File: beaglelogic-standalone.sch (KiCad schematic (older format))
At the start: 252 parts, among them J1 USB_OTG, J2 CONN_02X02, J3 USB_A, J4 CONN_01X06, J5 SI-51009-F, J6 CONN_02X12, J7 CONN_02X16, J8 Barrel_Jack, M1 TEST_1P, M2 TEST_1P, M3 TEST_1P, M4 TEST_1P, Q1 BSS138, Q2 BSS138, SW1 SW_PUSH_SMALL_H, SW2 SW_PUSH_SMALL_H, U1 74LVC1G07, U10 MCP79410/TDFN, U11 SST26VF064B, U12 TPS73101, U13 SN74LVCH16T245, U14 DVIULC6-4SC6, U15 DVIULC6-4SC6, U16 DVIULC6-4SC6, U17 DVIULC6-4SC6, U18 74LV1T125, U19 EMMC_4G, U2 AP1117, U3 TPS2051C, U4 TPD4S012, U5 TPD4S012, U6 OSD3358-SM, U7 KSZ9031RNXCC, U8 74LVC2G241, U9 74LVC1G125, Y1 25MHz, Y2 24MHz, Y3 32.768kHz,CL=9pF

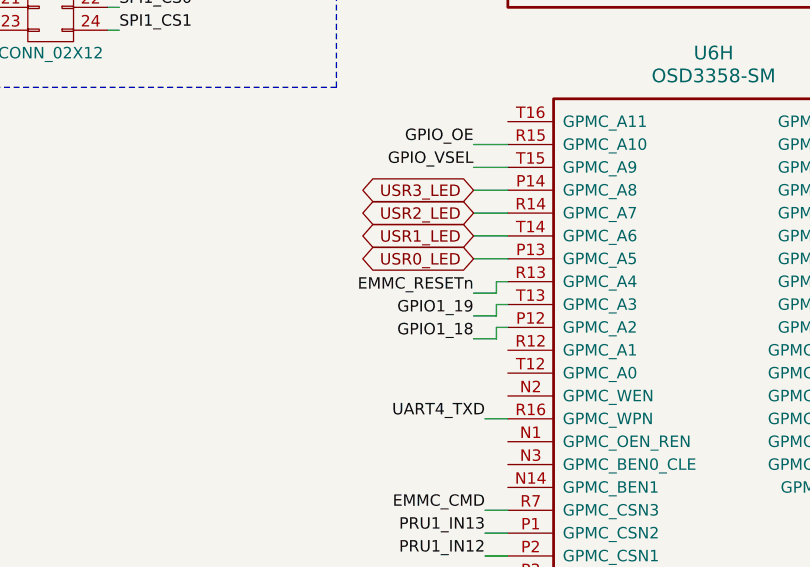
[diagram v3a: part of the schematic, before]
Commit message: Route the eMMC
Signed-off-by: Kumar Abhishek <abhishek@theembeddedkitchen.net>
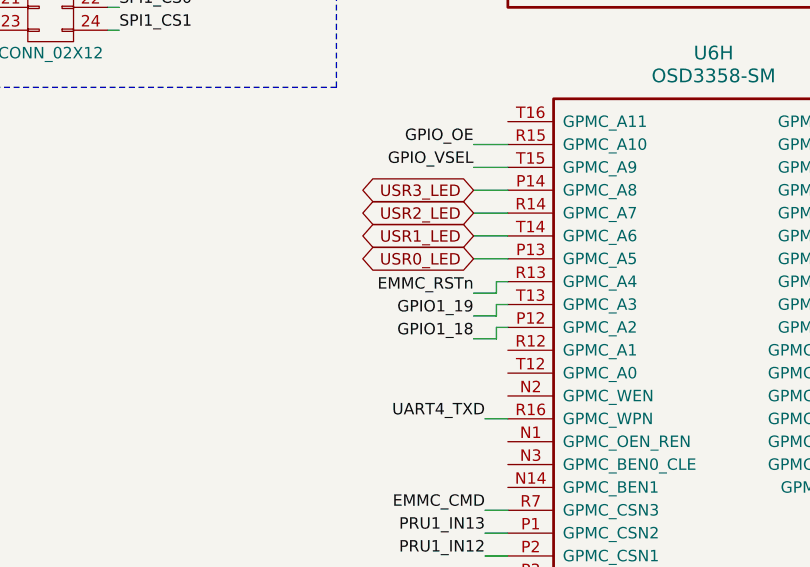
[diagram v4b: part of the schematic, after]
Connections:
- net EMMC_RESETn is gone; now on net EMMC_RSTn: U6.R13 (GPMC_A4)
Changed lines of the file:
@@
 GPIO_OE
 Text Label 9200 7200 2    50   ~ 0
-EMMC_RESETn
+EMMC_RSTn
 Text Label 12550 2700 2    50   ~ 0
 SPIF_CS

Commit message: Finish routing
Signed-off-by: Kumar Abhishek <abhishek@theembeddedkitchen.net>
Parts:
- added C65, C66: 0.1uF, Capacitors_SMD:C_0402, symbol C_Small
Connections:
- net +3V3: now also C65.2
- net DIN00: now also U14.4 (X3); no longer U14.1 (X1)
- net DIN03: now also U14.1 (X1); no longer U14.4 (X3)
- net DIN04: now also U15.4 (X3); no longer U15.1 (X1)
- net DIN07: now also U15.1 (X1); no longer U15.4 (X3)
- net DIN08: now also U16.4 (X3); no longer U16.1 (X1)
- net DIN11: now also U16.1 (X1); no longer U16.4 (X3)
- net DIN12: now also U17.4 (X3); no longer U17.1 (X1)
- net DIN15: now also U17.1 (X1); no longer U17.4 (X3)
- net GND: now also C65.1, C66.1
- net at C42.2, R58.1, U12.5 (VOUT)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: now also C66.2
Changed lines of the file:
@@
 	1    0    0    -1
 $EndComp
-Text Label 17900 5150 2    50   ~ 0
+Text Label 18800 5450 0    50   ~ 0
 DIN00
 Text Label 18800 5150 0    50   ~ 0
@@
 Text Label 17900 5450 2    50   ~ 0
 DIN02
-Text Label 18800 5450 0    50   ~ 0
+Text Label 17900 5150 2    50   ~ 0
 DIN03
-Text Label 17900 6000 2    50   ~ 0
+Text Label 18800 6300 0    50   ~ 0
 DIN04
 Text Label 18800 6000 0    50   ~ 0
@@
 Text Label 17900 6300 2    50   ~ 0
 DIN06
-Text Label 18800 6300 0    50   ~ 0
+Text Label 17900 6000 2    50   ~ 0
 DIN07
-Text Label 17900 6850 2    50   ~ 0
+Text Label 18800 7150 0    50   ~ 0
 DIN08
 Text Label 18800 6850 0    50   ~ 0
@@
 Text Label 17900 7150 2    50   ~ 0
 DIN10
-Text Label 18800 7150 0    50   ~ 0
+Text Label 17900 6850 2    50   ~ 0
 DIN11
-Text Label 17900 7750 2    50   ~ 0
+Text Label 18800 8050 0    50   ~ 0
 DIN12
 Text Label 18800 7750 0    50   ~ 0
 DIN13
-Text Label 18800 8050 0    50   ~ 0
+Text Label 17900 7750 2    50   ~ 0
 DIN15
 Text Label 17900 8050 2    50   ~ 0
@@
 L GND #PWR026
 U 1 1 59699004
-P 15000 5400
-F 0 "#PWR026" H 15000 5150 50  0001 C CNN
-F 1 "GND" H 15005 5227 50  0000 C CNN
-F 2 "" H 15000 5400 50  0001 C CNN
-F 3 "" H 15000 5400 50  0001 C CNN
-	1    15000 5400
+P 15000 5550
+F 0 "#PWR026" H 15000 5300 50  0001 C CNN
+F 1 "GND" H 15005 5377 50  0000 C CNN
+F 2 "" H 15000 5550 50  0001 C CNN
+F 3 "" H 15000 5550 50  0001 C CNN
+	1    15000 5550
 	1    0    0    -1
 $EndComp
@@
 	16700 4950 16700 5350
 Wire Wire Line
-	16400 5350 17100 5350
+	16400 5350 17300 5350
 Wire Wire Line
 	16400 5350 16400 5300
@@
 Connection ~ 16800 5350
 Wire Wire Line
-	17200 5000 17100 5000
+	17100 5000 17300 5000
 Wire Wire Line
 	17100 5000 17100 5100
@@
 Connection ~ 15300 5250
 Wire Wire Line
-	15000 5250 15000 5400
+	15000 5250 15000 5550
 Connection ~ 13300 5250
 Wire Wire Line
@@
 	1    0    0    -1
 $EndComp
+$Comp
+L C_Small C66
+U 1 1 59B026E5
+P 17300 5200
+F 0 "C66" H 17186 5154 50  0000 R CNN
+F 1 "0.1uF" H 17186 5245 50  0000 R CNN
+F 2 "Capacitors_SMD:C_0402" H 17338 5050 50  0001 C CNN
+F 3 "" H 17300 5200 50  0001 C CNN
+	1    17300 5200
+	-1   0    0    1
+$EndComp
+Wire Wire Line
+	17300 5000 17300 5100
+Wire Wire Line
+	17300 5350 17300 5300
+Connection ~ 17100 5350
+$Comp
+L C_Small C65
+U 1 1 59B047BC
+P 15150 5400
+F 0 "C65" V 14950 5400 50  0000 C CNN
+F 1 "0.1uF" V 15050 5400 50  0000 C CNN
+F 2 "Capacitors_SMD:C_0402" H 15188 5250 50  0001 C CNN
+F 3 "" H 15150 5400 50  0001 C CNN
+	1    15150 5400
+	0    -1   -1   0
+$EndComp
+Wire Wire Line
+	15050 5400 15000 5400
+Connection ~ 15000 5400
+Wire Wire Line
+	15250 5400 15300 5400
+Connection ~ 15300 5400
 $EndSCHEMATC

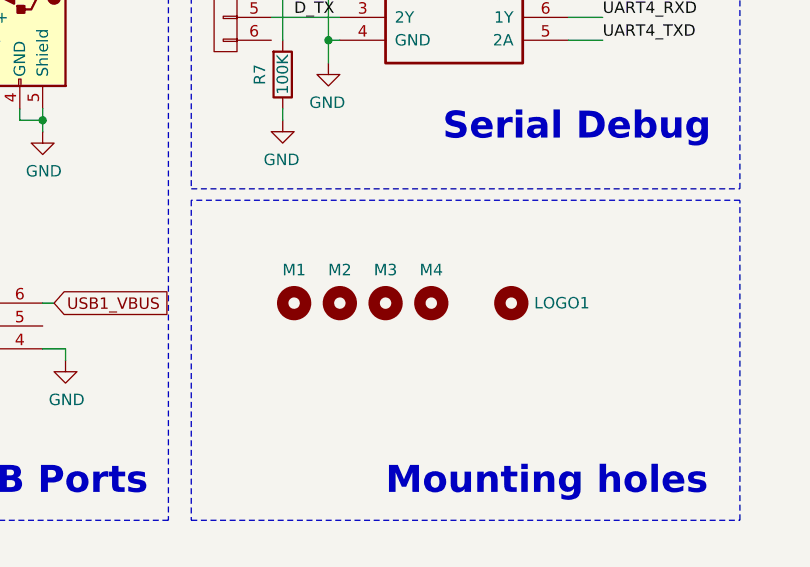
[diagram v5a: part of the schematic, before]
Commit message: Final touches to Rev A
 * Shrink logo to fit on board
 * Add fiducials on board
 * Rotate USB-A connector 90 degrees so that it does not interfere with
   microUSB
 * Add helper text

Signed-off-by: Kumar Abhishek <abhishek@theembeddedkitchen.net>
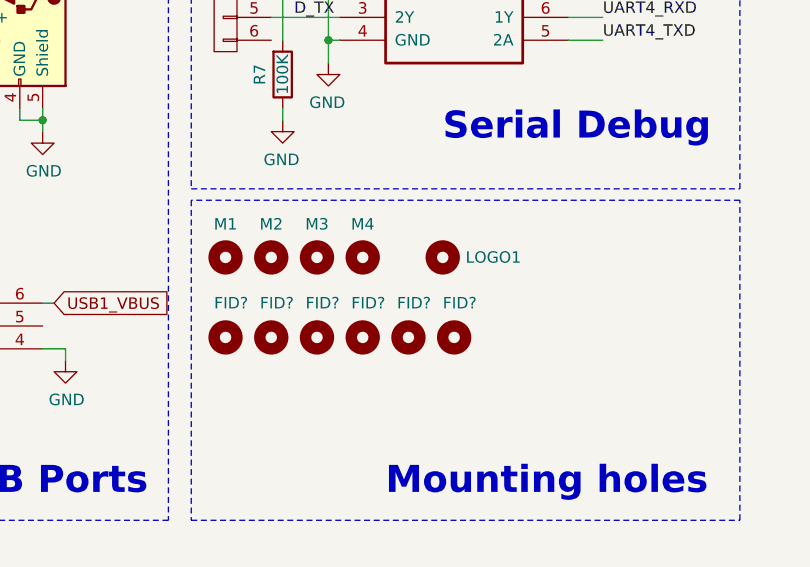
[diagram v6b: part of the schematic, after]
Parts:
- added FID? (x6): Mounting_Hole, Fiducials:Fiducial_1mm_Dia_2.54mm_Outer_CopperTop, symbol Mounting_Hole
- D1, D2, D3, D4: value LED -> GREEN
- R104, R106, R108, R110, R112, R114, R116, R118, R66, R68, R70, R72, R74, R76, R78, R80, R82: value 1M,DNI -> 1M,S
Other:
- moved on the sheet: LOGO1, M1, M2, M3, M4
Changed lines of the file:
@@
 P 19600 5200
 F 0 "R66" V 19600 5250 50  0000 R CNN
-F 1 "1M,DNI" V 19700 5300 50  0001 R CNN
+F 1 "1M,S" V 19700 5300 50  0001 R CNN
 F 2 "Resistors_SMD:R_0402" V 19530 5200 50  0001 C CNN
 F 3 "" H 19600 5200 50  0001 C CNN
@@
 P 19600 5650
 F 0 "R68" V 19600 5700 50  0000 R CNN
-F 1 "1M,DNI" V 19700 5750 50  0001 R CNN
+F 1 "1M,S" V 19700 5750 50  0001 R CNN
 F 2 "Resistors_SMD:R_0402" V 19530 5650 50  0001 C CNN
 F 3 "" H 19600 5650 50  0001 C CNN
@@
 P 19600 6100
 F 0 "R70" V 19600 6150 50  0000 R CNN
-F 1 "1M,DNI" V 19700 6200 50  0001 R CNN
+F 1 "1M,S" V 19700 6200 50  0001 R CNN
 F 2 "Resistors_SMD:R_0402" V 19530 6100 50  0001 C CNN
 F 3 "" H 19600 6100 50  0001 C CNN
@@
 P 19600 6550
 F 0 "R72" V 19600 6600 50  0000 R CNN
-F 1 "1M,DNI" V 19700 6650 50  0001 R CNN
+F 1 "1M,S" V 19700 6650 50  0001 R CNN
 F 2 "Resistors_SMD:R_0402" V 19530 6550 50  0001 C CNN
 F 3 "" H 19600 6550 50  0001 C CNN
@@
 P 19600 7000
 F 0 "R74" V 19600 7050 50  0000 R CNN
-F 1 "1M,DNI" V 19700 7100 50  0001 R CNN
+F 1 "1M,S" V 19700 7100 50  0001 R CNN
 F 2 "Resistors_SMD:R_0402" V 19530 7000 50  0001 C CNN
 F 3 "" H 19600 7000 50  0001 C CNN
@@
 P 19600 7450
 F 0 "R76" V 19600 7500 50  0000 R CNN
-F 1 "1M,DNI" V 19700 7550 50  0001 R CNN
+F 1 "1M,S" V 19700 7550 50  0001 R CNN
 F 2 "Resistors_SMD:R_0402" V 19530 7450 50  0001 C CNN
 F 3 "" H 19600 7450 50  0001 C CNN
@@
 P 19600 7900
 F 0 "R78" V 19600 7950 50  0000 R CNN
-F 1 "1M,DNI" V 19700 8000 50  0001 R CNN
+F 1 "1M,S" V 19700 8000 50  0001 R CNN
 F 2 "Resistors_SMD:R_0402" V 19530 7900 50  0001 C CNN
 F 3 "" H 19600 7900 50  0001 C CNN
@@
 P 19600 8350
 F 0 "R80" V 19600 8400 50  0000 R CNN
-F 1 "1M,DNI" V 19700 8450 50  0001 R CNN
+F 1 "1M,S" V 19700 8450 50  0001 R CNN
 F 2 "Resistors_SMD:R_0402" V 19530 8350 50  0001 C CNN
 F 3 "" H 19600 8350 50  0001 C CNN
@@
 P 20900 5200
 F 0 "R104" V 20900 5250 50  0000 R CNN
-F 1 "1M,DNI" V 21000 5300 50  0001 R CNN
+F 1 "1M,S" V 21000 5300 50  0001 R CNN
 F 2 "Resistors_SMD:R_0402" V 20830 5200 50  0001 C CNN
 F 3 "" H 20900 5200 50  0001 C CNN
@@
 P 20900 5650
 F 0 "R106" V 20900 5700 50  0000 R CNN
-F 1 "1M,DNI" V 21000 5750 50  0001 R CNN
+F 1 "1M,S" V 21000 5750 50  0001 R CNN
 F 2 "Resistors_SMD:R_0402" V 20830 5650 50  0001 C CNN
 F 3 "" H 20900 5650 50  0001 C CNN
@@
 P 20900 6100
 F 0 "R108" V 20900 6150 50  0000 R CNN
-F 1 "1M,DNI" V 21000 6200 50  0001 R CNN
+F 1 "1M,S" V 21000 6200 50  0001 R CNN
 F 2 "Resistors_SMD:R_0402" V 20830 6100 50  0001 C CNN
 F 3 "" H 20900 6100 50  0001 C CNN
@@
 P 20900 6550
 F 0 "R110" V 20900 6600 50  0000 R CNN
-F 1 "1M,DNI" V 21000 6650 50  0001 R CNN
+F 1 "1M,S" V 21000 6650 50  0001 R CNN
 F 2 "Resistors_SMD:R_0402" V 20830 6550 50  0001 C CNN
 F 3 "" H 20900 6550 50  0001 C CNN
@@
 P 20900 7000
 F 0 "R112" V 20900 7050 50  0000 R CNN
-F 1 "1M,DNI" V 21000 7100 50  0001 R CNN
+F 1 "1M,S" V 21000 7100 50  0001 R CNN
 F 2 "Resistors_SMD:R_0402" V 20830 7000 50  0001 C CNN
 F 3 "" H 20900 7000 50  0001 C CNN
@@
 P 20900 7450
 F 0 "R114" V 20900 7500 50  0000 R CNN
-F 1 "1M,DNI" V 21000 7550 50  0001 R CNN
+F 1 "1M,S" V 21000 7550 50  0001 R CNN
 F 2 "Resistors_SMD:R_0402" V 20830 7450 50  0001 C CNN
 F 3 "" H 20900 7450 50  0001 C CNN
@@
 P 20900 7900
 F 0 "R116" V 20900 7950 50  0000 R CNN
-F 1 "1M,DNI" V 21000 8000 50  0001 R CNN
+F 1 "1M,S" V 21000 8000 50  0001 R CNN
 F 2 "Resistors_SMD:R_0402" V 20830 7900 50  0001 C CNN
 F 3 "" H 20900 7900 50  0001 C CNN
@@
 P 20900 8350
 F 0 "R118" V 20900 8400 50  0000 R CNN
-F 1 "1M,DNI" V 21000 8450 50  0001 R CNN
+F 1 "1M,S" V 21000 8450 50  0001 R CNN
 F 2 "Resistors_SMD:R_0402" V 20830 8350 50  0001 C CNN
 F 3 "" H 20900 8350 50  0001 C CNN
@@
 P 6000 1250
 F 0 "D4" H 6000 1200 50  0000 C CNN
-F 1 "LED" H 6000 1350 50  0001 C CNN
+F 1 "GREEN" H 6000 1350 50  0001 C CNN
 F 2 "LEDs:LED_0603" H 6000 1250 50  0001 C CNN
 F 3 "" H 6000 1250 50  0001 C CNN
@@
 P 6000 1050
 F 0 "D3" H 6000 1000 50  0000 C CNN
-F 1 "LED" H 6000 1150 50  0001 C CNN
+F 1 "GREEN" H 6000 1150 50  0001 C CNN
 F 2 "LEDs:LED_0603" H 6000 1050 50  0001 C CNN
 F 3 "" H 6000 1050 50  0001 C CNN
@@
 P 6000 850
 F 0 "D2" H 6000 800 50  0000 C CNN
-F 1 "LED" H 6000 950 50  0001 C CNN
+F 1 "GREEN" H 6000 950 50  0001 C CNN
 F 2 "LEDs:LED_0603" H 6000 850 50  0001 C CNN
 F 3 "" H 6000 850 50  0001 C CNN
@@
 P 6000 650
 F 0 "D1" H 6000 600 50  0000 C CNN
-F 1 "LED" H 6000 750 50  0001 C CNN
+F 1 "GREEN" H 6000 750 50  0001 C CNN
 F 2 "LEDs:LED_0603" H 6000 650 50  0001 C CNN
 F 3 "" H 6000 650 50  0001 C CNN
@@
 P 19600 8800
 F 0 "R82" V 19600 8850 50  0000 R CNN
-F 1 "1M,DNI" V 19700 8900 50  0001 R CNN
+F 1 "1M,S" V 19700 8900 50  0001 R CNN
 F 2 "Resistors_SMD:R_0402" V 19530 8800 50  0001 C CNN
 F 3 "" H 19600 8800 50  0001 C CNN
@@
 L Mounting_Hole M1
 U 1 1 59A18719
-P 4550 11750
-F 0 "M1" H 4550 11895 50  0000 C CNN
-F 1 "TEST_1P" H 4608 11779 50  0001 L CNN
-F 2 "Mounting_Holes:MountingHole_3.2mm_M3" H 4750 11750 50  0001 C CNN
-F 3 "" H 4750 11750 50  0001 C CNN
-	1    4550 11750
+P 4250 11550
+F 0 "M1" H 4250 11695 50  0000 C CNN
+F 1 "TEST_1P" H 4308 11579 50  0001 L CNN
+F 2 "Mounting_Holes:MountingHole_3.2mm_M3" H 4450 11550 50  0001 C CNN
+F 3 "" H 4450 11550 50  0001 C CNN
+	1    4250 11550
 	1    0    0    -1
 $EndComp
@@
 L Mounting_Hole M2
 U 1 1 59A1A3C5
-P 4750 11750
-F 0 "M2" H 4750 11895 50  0000 C CNN
-F 1 "TEST_1P" H 4808 11779 50  0001 L CNN
-F 2 "Mounting_Holes:MountingHole_3.2mm_M3" H 4950 11750 50  0001 C CNN
-F 3 "" H 4950 11750 50  0001 C CNN
-	1    4750 11750
+P 4450 11550
+F 0 "M2" H 4450 11695 50  0000 C CNN
+F 1 "TEST_1P" H 4508 11579 50  0001 L CNN
+F 2 "Mounting_Holes:MountingHole_3.2mm_M3" H 4650 11550 50  0001 C CNN
+F 3 "" H 4650 11550 50  0001 C CNN
+	1    4450 11550
 	1    0    0    -1
 $EndComp
@@
 L Mounting_Hole M3
 U 1 1 59A1A5E5
-P 4950 11750
-F 0 "M3" H 4950 11895 50  0000 C CNN
-F 1 "TEST_1P" H 5008 11779 50  0001 L CNN
-F 2 "Mounting_Holes:MountingHole_3.2mm_M3" H 5150 11750 50  0001 C CNN
-F 3 "" H 5150 11750 50  0001 C CNN
-	1    4950 11750
+P 4650 11550
+F 0 "M3" H 4650 11695 50  0000 C CNN
+F 1 "TEST_1P" H 4708 11579 50  0001 L CNN
+F 2 "Mounting_Holes:MountingHole_3.2mm_M3" H 4850 11550 50  0001 C CNN
+F 3 "" H 4850 11550 50  0001 C CNN
+	1    4650 11550
 	1    0    0    -1
 $EndComp
@@
 L Mounting_Hole LOGO1
 U 1 1 59A1CFE2
-P 5500 11750
-F 0 "LOGO1" H 5600 11750 50  0000 L CNN
-F 1 "TEST_1P" H 5558 11779 50  0001 L CNN
-F 2 "beaglelogic-standalone:beaglelogic-logo" H 5700 11750 50  0001 C CNN
-F 3 "" H 5700 11750 50  0001 C CNN
-	1    5500 11750
+P 5200 11550
+F 0 "LOGO1" H 5300 11550 50  0000 L CNN
+F 1 "TEST_1P" H 5258 11579 50  0001 L CNN
+F 2 "beaglelogic-standalone:beaglelogic-logo" H 5400 11550 50  0001 C CNN
+F 3 "" H 5400 11550 50  0001 C CNN
+	1    5200 11550
 	1    0    0    -1
 $EndComp
@@
 L Mounting_Hole M4
 U 1 1 59A3557F
-P 5150 11750
-F 0 "M4" H 5150 11895 50  0000 C CNN
-F 1 "TEST_1P" H 5208 11779 50  0001 L CNN
-F 2 "Mounting_Holes:MountingHole_3.2mm_M3" H 5350 11750 50  0001 C CNN
-F 3 "" H 5350 11750 50  0001 C CNN
-	1    5150 11750
+P 4850 11550
+F 0 "M4" H 4850 11695 50  0000 C CNN
+F 1 "TEST_1P" H 4908 11579 50  0001 L CNN
+F 2 "Mounting_Holes:MountingHole_3.2mm_M3" H 5050 11550 50  0001 C CNN
+F 3 "" H 5050 11550 50  0001 C CNN
+	1    4850 11550
 	1    0    0    -1
 $EndComp
@@
 	15250 5400 15300 5400
 Connection ~ 15300 5400
+$Comp
+L Mounting_Hole FID?
+U 1 1 59B3CD1D
+P 4250 11900
+F 0 "FID?" H 4200 12050 50  0000 L CNN
+F 1 "Mounting_Hole" H 4350 11855 50  0001 L CNN
+F 2 "Fiducials:Fiducial_1mm_Dia_2.54mm_Outer_CopperTop" H 4250 11900 50  0001 C CNN
+F 3 "" H 4250 11900 50  0001 C CNN
+	1    4250 11900
+	1    0    0    -1
+$EndComp
+$Comp
+L Mounting_Hole FID?
+U 1 1 59B3EE5D
+P 4450 11900
+F 0 "FID?" H 4400 12050 50  0000 L CNN
+F 1 "Mounting_Hole" H 4550 11855 50  0001 L CNN
+F 2 "Fiducials:Fiducial_1mm_Dia_2.54mm_Outer_CopperTop" H 4450 11900 50  0001 C CNN
+F 3 "" H 4450 11900 50  0001 C CNN
+	1    4450 11900
+	1    0    0    -1
+$EndComp
+$Comp
+L Mounting_Hole FID?
+U 1 1 59B3F087
+P 4650 11900
+F 0 "FID?" H 4600 12050 50  0000 L CNN
+F 1 "Mounting_Hole" H 4750 11855 50  0001 L CNN
+F 2 "Fiducials:Fiducial_1mm_Dia_2.54mm_Outer_CopperTop" H 4650 11900 50  0001 C CNN
+F 3 "" H 4650 11900 50  0001 C CNN
+	1    4650 11900
+	1    0    0    -1
+$EndComp
+$Comp
+L Mounting_Hole FID?
+U 1 1 59B3F2B7
+P 4850 11900
+F 0 "FID?" H 4800 12050 50  0000 L CNN
+F 1 "Mounting_Hole" H 4950 11855 50  0001 L CNN
+F 2 "Fiducials:Fiducial_1mm_Dia_2.54mm_Outer_CopperTop" H 4850 11900 50  0001 C CNN
+F 3 "" H 4850 11900 50  0001 C CNN
+	1    4850 11900
+	1    0    0    -1
+$EndComp
+$Comp
+L Mounting_Hole FID?
+U 1 1 59B3F4E9
+P 5050 11900
+F 0 "FID?" H 5000 12050 50  0000 L CNN
+F 1 "Mounting_Hole" H 5150 11855 50  0001 L CNN
+F 2 "Fiducials:Fiducial_1mm_Dia_2.54mm_Outer_CopperTop" H 5050 11900 50  0001 C CNN
+F 3 "" H 5050 11900 50  0001 C CNN
+	1    5050 11900
+	1    0    0    -1
+$EndComp
+$Comp
+L Mounting_Hole FID?
+U 1 1 59B3F71B
+P 5250 11900
+F 0 "FID?" H 5200 12050 50  0000 L CNN
+F 1 "Mounting_Hole" H 5350 11855 50  0001 L CNN
+F 2 "Fiducials:Fiducial_1mm_Dia_2.54mm_Outer_CopperTop" H 5250 11900 50  0001 C CNN
+F 3 "" H 5250 11900 50  0001 C CNN
+	1    5250 11900
+	1    0    0    -1
+$EndComp
 $EndSCHEMATC

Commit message: Release Candidate
 * Fix incorrect footprint for MCP79410
 * Adjust footprint for KSZ9031 adding more thermal vias in EP and modifying
   paste pattern
 * Add helper text
 * Add vias to some unused signals for testing purposes

Signed-off-by: Kumar Abhishek <abhishek@theembeddedkitchen.net>
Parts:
- J1: footprint beaglelogic-standalone:USB_MICRO_B_ST-USB-001E -> beaglelogic-standalone:10118192-0001LF
- U10: footprint Housings_DFN_QFN:DFN-8-1EP_2x3mm_Pitch0.5mm -> beaglelogic-standalone:DFN-8-1EP_3x2mm
- U7: footprint Housings_DFN_QFN:QFN-48-1EP_7x7mm_Pitch0.5mm -> beaglelogic-standalone:QFN-48-1EP_7x7mm
- gave numbers to parts that had none: 6
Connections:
- net GND: now also U6.A9 (AGND_ADC), U6.B9 (VREFN)
- net VDD_1V8: now also U6.F10 (SYS_VDD_1P8V_F10), U6.G10 (SYS_VDD_1P8V_G10), U6.H10 (SYS_VDD_1P8V_H10), U6.H11 (SYS_VDD_1P8V_H11), U6.J10 (SYS_VDD_1P8V_J10), U6.J11 (SYS_VDD_1P8V_J11)
- net VDD_ADC: now reaches U6.B7 (VREFP)
- net VDD_ADC: now also U6.A7 (SYS_ADC_1P8V)
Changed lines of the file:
@@
 F 0 "J1" H 855 12267 50  0000 C CNN
 F 1 "USB_OTG" H 855 12176 50  0000 C CNN
-F 2 "beaglelogic-standalone:USB_MICRO_B_ST-USB-001E" H 950 11750 50  0001 C CNN
+F 2 "beaglelogic-standalone:10118192-0001LF" H 950 11750 50  0001 C CNN
 F 3 "" H 950 11750 50  0001 C CNN
 	1    800  11800
@@
 F 0 "U7" H 3600 8687 60  0000 C CNN
 F 1 "KSZ9031RNXCC" H 3600 8581 60  0000 C CNN
-F 2 "Housings_DFN_QFN:QFN-48-1EP_7x7mm_Pitch0.5mm" H 2600 5000 60  0001 C CNN
+F 2 "beaglelogic-standalone:QFN-48-1EP_7x7mm" H 2600 5000 60  0001 C CNN
 F 3 "" H 2600 5000 60  0001 C CNN
 	1    3600 6800
@@
 F 0 "U10" H 13350 1928 50  0000 C CNN
 F 1 "MCP79410/TDFN" H 13350 1837 50  0000 C CNN
-F 2 "Housings_DFN_QFN:DFN-8-1EP_2x3mm_Pitch0.5mm" H 13350 1500 50  0001 C CNN
+F 2 "beaglelogic-standalone:DFN-8-1EP_3x2mm" H 13350 1500 50  0001 C CNN
 F 3 "DOCUMENTATION" H 13350 1500 50  0001 C CNN
 	1    13350 1500
@@
 	19750 12300 19850 12300
 Wire Wire Line
-	19850 12300 19850 12200
+	19850 12200 19850 12900
 Connection ~ 19850 12200
 Wire Wire Line
@@
 Connection ~ 15300 5400
 $Comp
-L Mounting_Hole FID?
+L Mounting_Hole FID1
 U 1 1 59B3CD1D
 P 4250 11900
-F 0 "FID?" H 4200 12050 50  0000 L CNN
+F 0 "FID1" H 4200 12050 50  0000 L CNN
 F 1 "Mounting_Hole" H 4350 11855 50  0001 L CNN
 F 2 "Fiducials:Fiducial_1mm_Dia_2.54mm_Outer_CopperTop" H 4250 11900 50  0001 C CNN
@@
 $EndComp
 $Comp
-L Mounting_Hole FID?
+L Mounting_Hole FID2
 U 1 1 59B3EE5D
 P 4450 11900
-F 0 "FID?" H 4400 12050 50  0000 L CNN
+F 0 "FID2" H 4400 12050 50  0000 L CNN
 F 1 "Mounting_Hole" H 4550 11855 50  0001 L CNN
 F 2 "Fiducials:Fiducial_1mm_Dia_2.54mm_Outer_CopperTop" H 4450 11900 50  0001 C CNN
@@
 $EndComp
 $Comp
-L Mounting_Hole FID?
+L Mounting_Hole FID3
 U 1 1 59B3F087
 P 4650 11900
-F 0 "FID?" H 4600 12050 50  0000 L CNN
+F 0 "FID3" H 4600 12050 50  0000 L CNN
 F 1 "Mounting_Hole" H 4750 11855 50  0001 L CNN
 F 2 "Fiducials:Fiducial_1mm_Dia_2.54mm_Outer_CopperTop" H 4650 11900 50  0001 C CNN
@@
 $EndComp
 $Comp
-L Mounting_Hole FID?
+L Mounting_Hole FID4
 U 1 1 59B3F2B7
 P 4850 11900
-F 0 "FID?" H 4800 12050 50  0000 L CNN
+F 0 "FID4" H 4800 12050 50  0000 L CNN
 F 1 "Mounting_Hole" H 4950 11855 50  0001 L CNN
 F 2 "Fiducials:Fiducial_1mm_Dia_2.54mm_Outer_CopperTop" H 4850 11900 50  0001 C CNN
@@
 $EndComp
 $Comp
-L Mounting_Hole FID?
+L Mounting_Hole FID5
 U 1 1 59B3F4E9
 P 5050 11900
-F 0 "FID?" H 5000 12050 50  0000 L CNN
+F 0 "FID5" H 5000 12050 50  0000 L CNN
 F 1 "Mounting_Hole" H 5150 11855 50  0001 L CNN
 F 2 "Fiducials:Fiducial_1mm_Dia_2.54mm_Outer_CopperTop" H 5050 11900 50  0001 C CNN
@@
 $EndComp
 $Comp
-L Mounting_Hole FID?
+L Mounting_Hole FID6
 U 1 1 59B3F71B
 P 5250 11900
-F 0 "FID?" H 5200 12050 50  0000 L CNN
+F 0 "FID6" H 5200 12050 50  0000 L CNN
 F 1 "Mounting_Hole" H 5350 11855 50  0001 L CNN
 F 2 "Fiducials:Fiducial_1mm_Dia_2.54mm_Outer_CopperTop" H 5250 11900 50  0001 C CNN
@@
 	1    0    0    -1
 $EndComp
+Wire Wire Line
+	19850 12900 19750 12900
+Connection ~ 19850 12300
+Wire Wire Line
+	19750 12400 19850 12400
+Connection ~ 19850 12400
+Wire Wire Line
+	19750 12500 19850 12500
+Connection ~ 19850 12500
+Wire Wire Line
+	19750 12600 19850 12600
+Connection ~ 19850 12600
+Wire Wire Line
+	19750 12700 19850 12700
+Connection ~ 19850 12700
+Wire Wire Line
+	19750 12800 19850 12800
+Connection ~ 19850 12800
+$Comp
+L GND #PWR098
+U 1 1 59B6AA4A
+P 20350 11050
+F 0 "#PWR098" H 20350 10800 50  0001 C CNN
+F 1 "GND" H 20355 10877 50  0000 C CNN
+F 2 "" H 20350 11050 50  0001 C CNN
+F 3 "" H 20350 11050 50  0001 C CNN
+	1    20350 11050
+	1    0    0    -1
+$EndComp
+Wire Wire Line
+	20250 10950 20350 10950
+Wire Wire Line
+	20350 9950 20350 11050
+Wire Wire Line
+	20250 10850 20450 10850
+Text Label 20450 10850 0    50   ~ 0
+VDD_ADC
+Wire Wire Line
+	20250 9950 20350 9950
+Connection ~ 20350 10950
+Text Label 20000 13000 0    50   ~ 0
+VDD_ADC
+Wire Wire Line
+	19750 13000 20000 13000
 $EndSCHEMATC
